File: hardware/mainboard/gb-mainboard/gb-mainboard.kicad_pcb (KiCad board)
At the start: 2 copper layers, 77.4 x 81 mm, 55 parts, among them P101 NUCLEO-CN7, P102 NUCLEO-CN10, P103 MOTOR_SX, P104 MOTOR_DX, P105 WE-632723300011, P106 BATTERY, P107 EN_JMP, P108 BOOT_JMP, P109 ESP_PROG, Q101 DMP2120U-7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

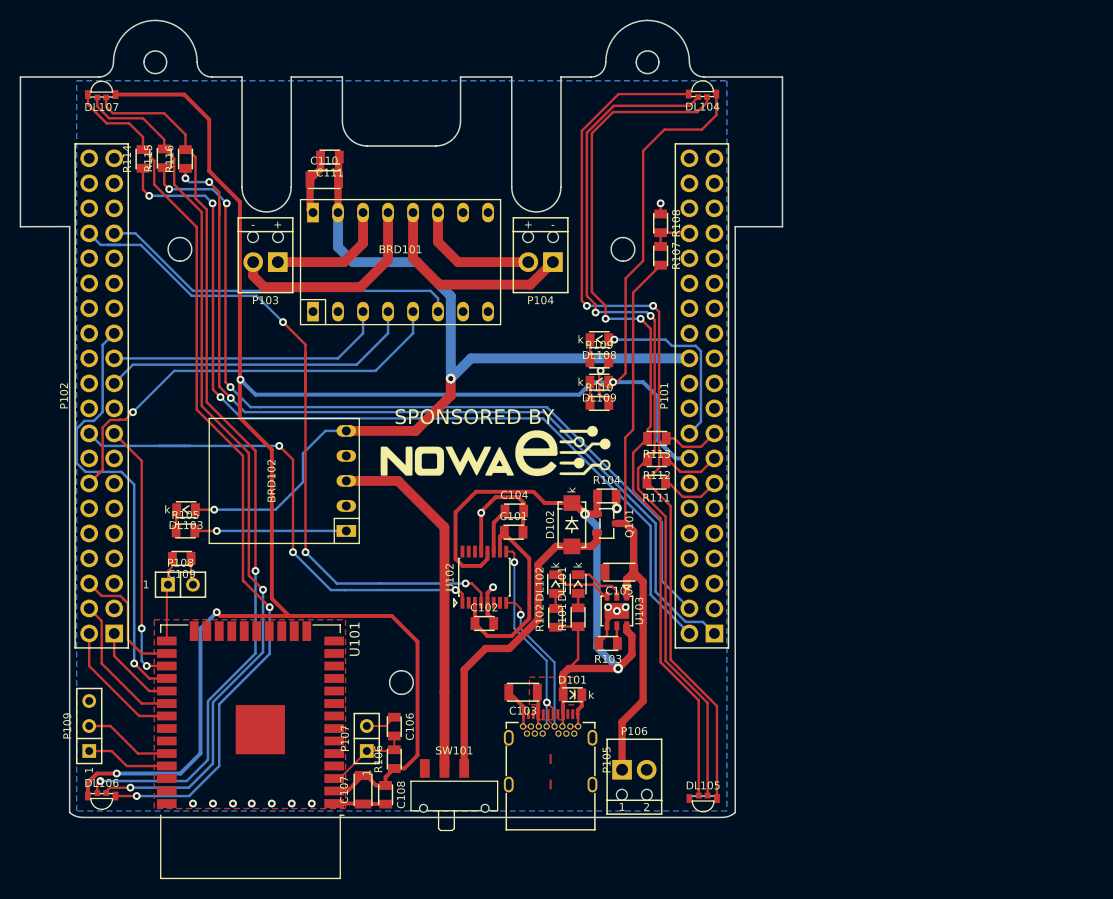
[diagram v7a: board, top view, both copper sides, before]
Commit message: Fixed PCB. Logo missing.
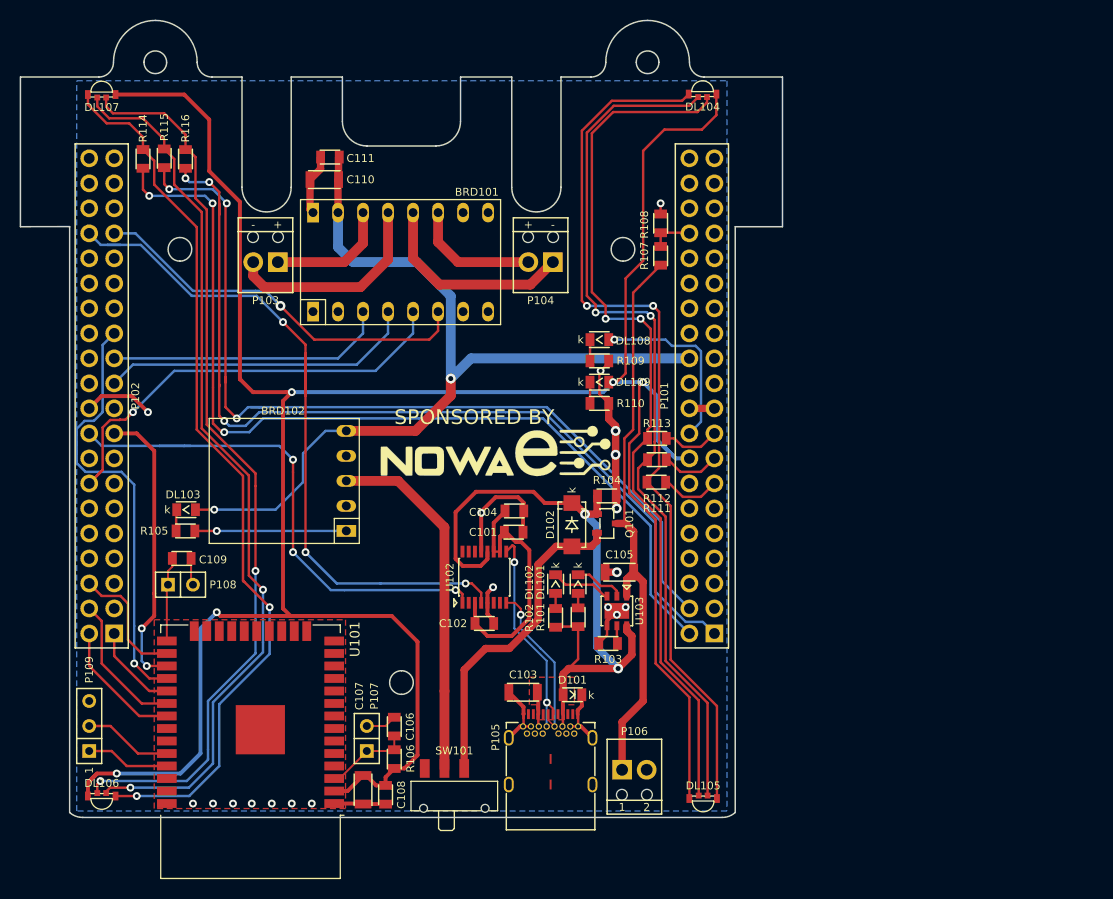
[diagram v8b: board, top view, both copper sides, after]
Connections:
- P101 pad 19: Net-(P101-Pad19) -> GND
- P101 pad 8: Net-(P101-Pad8) -> GND
- P102 pad 20: Net-(P102-Pad20) -> GND
- P102 pad 9: Net-(P102-Pad9) -> GND
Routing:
- net +3.3V: track 235.2 -> 277.6 mm, vias 4 -> 5
- net GND: track 54.5 -> 78.9 mm, vias 15 -> 19
- net /LED_LX_GREEN: track 87.2 -> 91.3 mm
- net /LED_LX_RED: track 91.5 -> 94.6 mm
- net /LED_LX_BLUE: track 90.7 -> 93.8 mm
- net /MOTOR_DX_CTR1: track 37.0 -> 39.7 mm, vias 0 -> 1
- net /UART_CMD_TX: track 27.0 -> 29.4 mm
- net Net-(C101-Pad1): track 25.5 -> 26.5 mm
- net /USB_DM: track 21.3 -> 22.2 mm
